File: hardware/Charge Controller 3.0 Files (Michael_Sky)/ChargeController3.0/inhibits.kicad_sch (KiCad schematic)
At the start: 18 parts, among them J10 SOL_TEST_01x01_Pin, J11 GND_TEST_01x01_Pin, J19 SYS-1x2, J2 SP_01x02_Pin, J3 BATT_TEST_01x01_Pin, J5 BATT_01x02_Pin, J9 SYS_TEST_01x01_Pin, Q1 SI2318CDS-T1-GE3, Q10 SI2318CDS-T1-GE3, Q11 SI2318CDS-T1-GE3, Q2 SI2318CDS-T1-GE3, Q3 SI2318CDS-T1-GE3, Q4 SI2318CDS-T1-GE3, Q9 SI2318CDS-T1-GE3, SW1 100SP1T1B1M1QEH

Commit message: New formatting
New formatting
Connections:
- net EN: now also SW1.2; no longer SW1.1
- net at D7.C, D9.C: now also SW1.1; no longer SW1.2
- net SOL_PIN: now reaches D7.A, J10.1 (Pin_1), J2.1 (Pin_1), Q1.3
- net SYS_PIN: now reaches J19.1 (Pin_1), J9.1 (Pin_1)
- net SYS_PIN: now also Q10.2; no longer Q10.3
- net at Q11.2: now also Q10.3; no longer Q10.2
- net SOL renamed IN
- net IN: no longer Q3.2
- net SYS/BATT renamed BATT_PIN
- net BATT_PIN: no longer Q11.3
- new net OUT: Q11.3, Q3.2
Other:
- moved on the sheet: J11, Q10, SW1

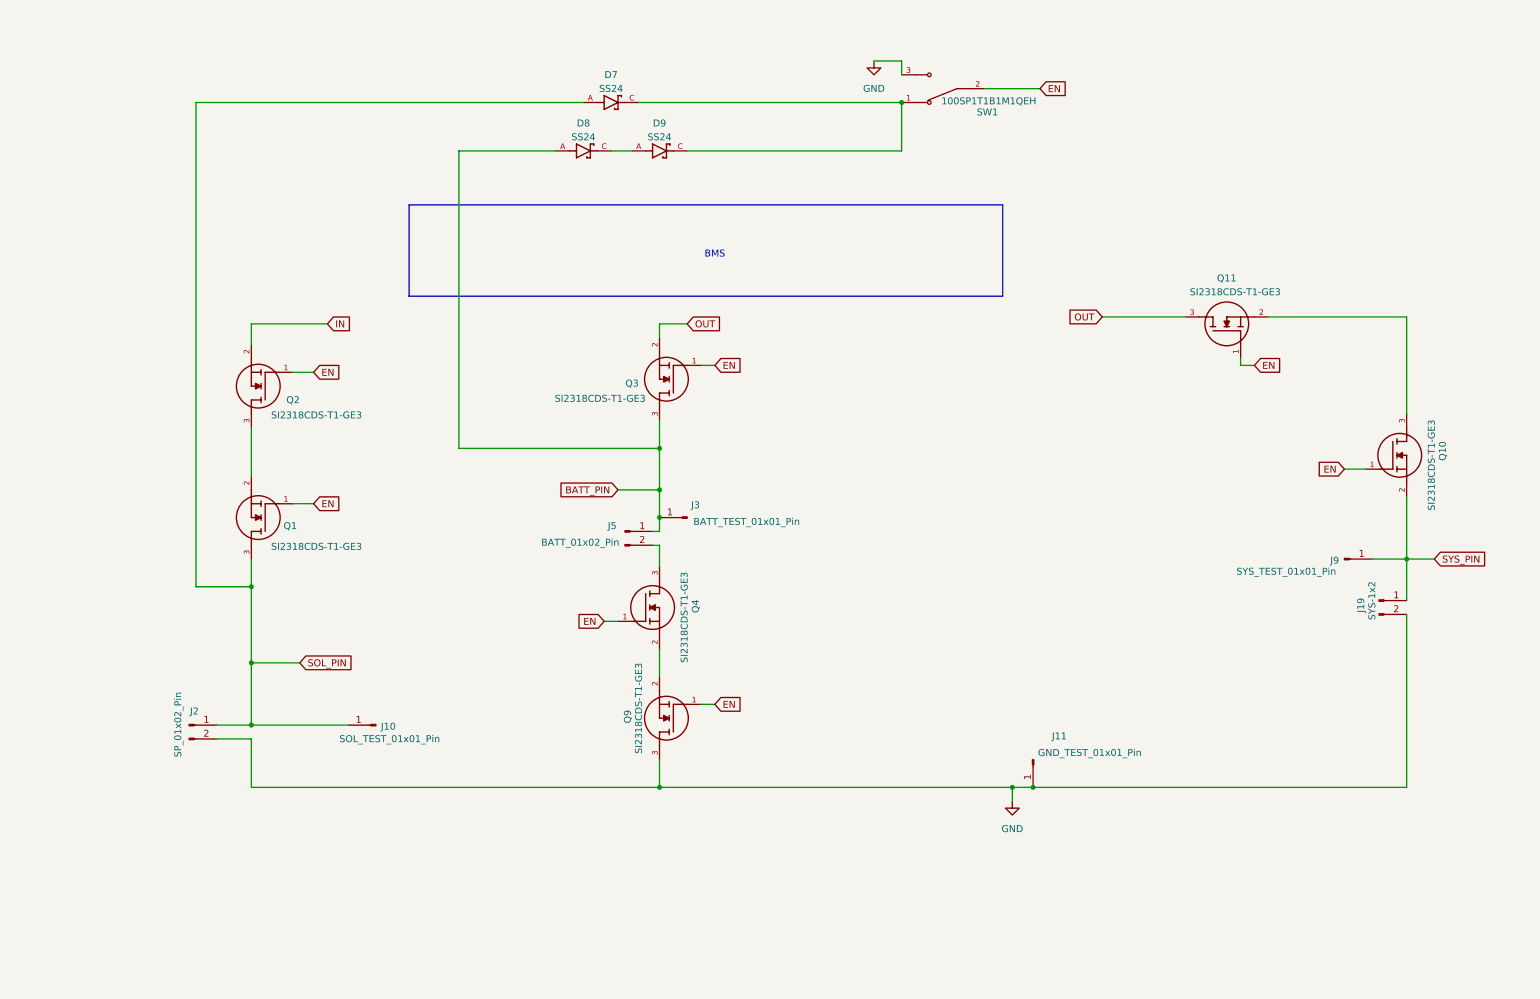
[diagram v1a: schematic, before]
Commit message: Final PCB?
inhibits rework, filtering rework
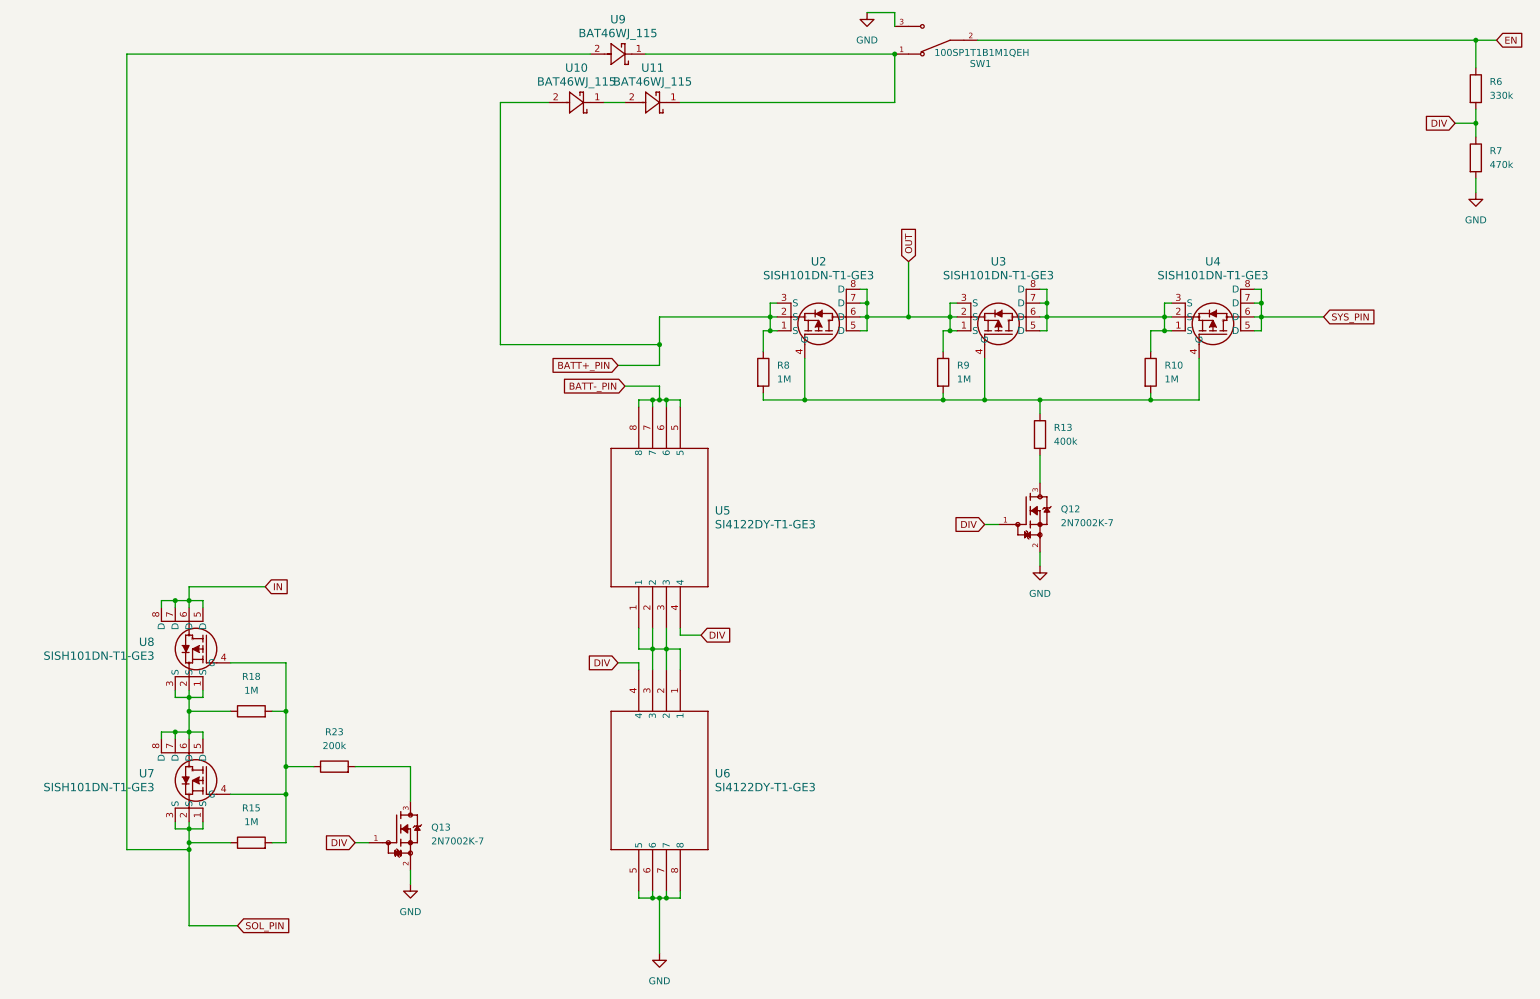
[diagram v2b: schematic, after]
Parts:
- removed D7, D8, D9: SS24, bmsfootprints:SS24, symbol SS24:SS24
- removed J10: SOL_TEST_01x01_Pin, Connector_PinHeader_2.54mm:PinHeader_1x01_P2.54mm_Vertical, symbol Connector:Conn_01x01_Pin
- removed J11: GND_TEST_01x01_Pin, Connector_PinHeader_2.54mm:PinHeader_1x01_P2.54mm_Vertical, symbol Connector:Conn_01x01_Pin
- removed J19: SYS-1x2, Connector_PinHeader_2.54mm:PinHeader_1x02_P2.54mm_Vertical, symbol Connector:Conn_01x02_Pin
- removed J2: SP_01x02_Pin, Connector_PinHeader_2.54mm:PinHeader_1x02_P2.54mm_Vertical, symbol Connector:Conn_01x02_Pin
- removed J3: BATT_TEST_01x01_Pin, Connector_PinHeader_2.54mm:PinHeader_1x01_P2.54mm_Vertical, symbol Connector:Conn_01x01_Pin
- removed J5: BATT_01x02_Pin, Connector_PinHeader_2.54mm:PinHeader_1x02_P2.54mm_Vertical, symbol Connector:Conn_01x02_Pin
- removed J9: SYS_TEST_01x01_Pin, Connector_PinHeader_2.54mm:PinHeader_1x01_P2.54mm_Vertical, symbol Connector:Conn_01x01_Pin
- removed Q1, Q10, Q11, Q2, Q3, Q4, Q9: SI2318CDS-T1-GE3, bmsfootprints:SI2318CDS-T1-GE3, symbol SI2318CDS-T1-GE3:SI2318CDS-T1-GE3
- added Q12, Q13: 2N7002K-7, bmsfootprints:2N7002K-7, symbol 2N7002K-7:2N7002K-7
- added R10, R15, R18, R8, R9: 1M, Resistor_SMD:R_0402_1005Metric, symbol Device:R
- added R13: 400k, Resistor_SMD:R_0805_2012Metric, symbol Device:R
- added R23: 200k, Resistor_SMD:R_0402_1005Metric, symbol Device:R
- added R6: 330k, Resistor_SMD:R_1206_3216Metric, symbol Device:R
- added R7: 470k, Resistor_SMD:R_1206_3216Metric, symbol Device:R
- added U10, U11, U9: BAT46WJ_115, bmsfootprints:BAT46WJ115, symbol BAT46WJ115:BAT46WJ_115
- added U2, U3, U4, U7, U8: SISH101DN-T1-GE3, bmsfootprints:SISH, symbol SISH101DN_T1_GE3:SISH101DN-T1-GE3
- added U5, U6: SI4122DY-T1-GE3, bmsfootprints:SI4122., symbol SI4122:SI4122DY-T1-GE3
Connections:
- net EN: now also R6.1
- net GND: now also Q12.2, Q13.2, R7.2, U6.5, U6.6, U6.7, U6.8
- net IN: now also U8.5 (D), U8.6 (D), U8.7 (D), U8.8 (D)
- net OUT: now also R9.1, U2.5 (D), U2.6 (D), U2.7 (D), U2.8 (D), U3.1 (S), U3.2 (S), U3.3 (S)
- net SOL_PIN: now also R15.1, U7.1 (S), U7.2 (S), U7.3 (S), U9.2
- net SYS_PIN: now also U4.5 (D), U4.6 (D), U4.7 (D), U4.8 (D)
- net at SW1.1: now also U11.1, U9.1
- new net: R15.2, R18.2, R23.1, U7.4 (G), U8.4 (G)
- new net: Q13.3, R23.2
- new net: R18.1, U7.5 (D), U7.6 (D), U7.7 (D), U7.8 (D), U8.1 (S), U8.2 (S), U8.3 (S)
- new net: U5.1, U5.2, U5.3, U6.1, U6.2, U6.3
- new net: Q12.3, R13.2
- new net: R10.2, R13.1, R8.2, R9.2, U2.4 (G), U3.4 (G), U4.4 (G)
- new net: U10.1, U11.2
- new net: R10.1, U3.5 (D), U3.6 (D), U3.7 (D), U3.8 (D), U4.1 (S), U4.2 (S), U4.3 (S)
- new net BATT+_PIN: R8.1, U10.2, U2.1 (S), U2.2 (S), U2.3 (S)
- new net BATT-_PIN: U5.5, U5.6, U5.7, U5.8
- new net DIV: Q12.1, Q13.1, R6.2, R7.1, U5.4, U6.4
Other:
- note removed: "BMS"
- moved on the sheet: SW1

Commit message: Sims + Gerbers added
Sims + Gerbers added
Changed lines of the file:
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@@
 	(wire
 		(pts
-			(xy 119.38 82.55) (xy 113.03 82.55)
+			(xy 119.38 82.55) (xy 111.76 82.55)
 		)
 		(stroke
@@
 	(global_label "BATT-_PIN"
 		(shape input)
-		(at 113.03 82.55 180)
+		(at 111.76 82.55 180)
 		(fields_autoplaced yes)
 		(effects
@@
 		)
 		(property "Intersheetrefs" "${INTERSHEET_REFS}"
-			(at 100.0057 82.55 0)
+			(at 98.7357 82.55 0)
 			(hide yes)
 			(show_name no)
